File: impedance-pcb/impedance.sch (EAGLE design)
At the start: 26 parts, among them U3 ADG704BRMZ, U4 ADG787BRMZ, U5 RED

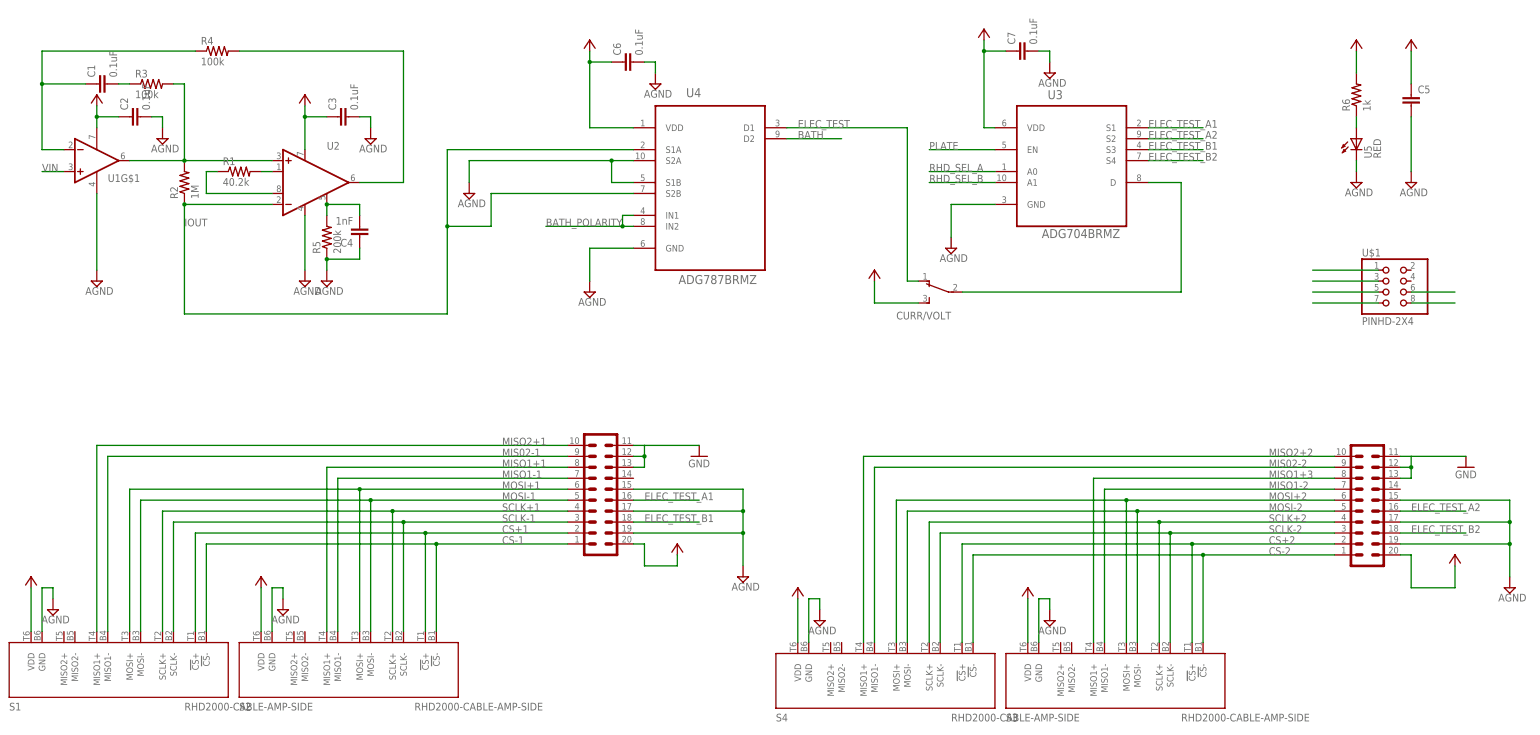
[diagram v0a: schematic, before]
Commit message: Created plating/impedance testing circuit. Need to get parts to prototype it.
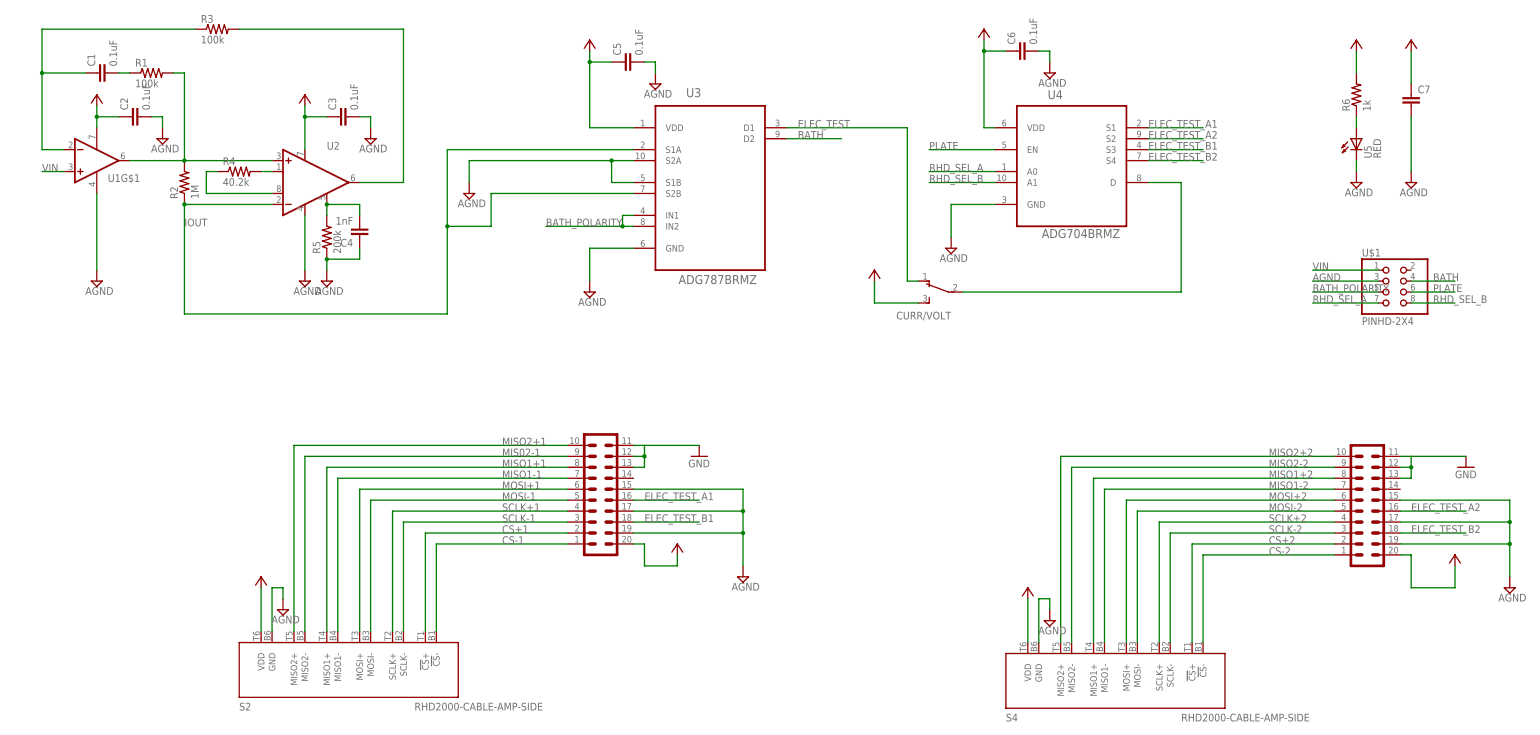
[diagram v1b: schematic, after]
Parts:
- removed S1, S3: RHD2000-CABLE-AMP-SIDE, RHD2000:RHD2000-CABLE-AMP-SIDE
- C5: value (none) -> 0.1uF; device impedance:C_1206 -> impedance:C_0805
- C7: value 0.1uF -> (none); device impedance:C_0805 -> impedance:C_1206
- R1: value 40.2k -> 100k
- R4: value 100k -> 40.2k
- U3: value ADG704BRMZ -> ADG787BRMZ; device impedance:ADG704BRMZ -> impedance:ADG787BRMZ
- U4: value ADG787BRMZ -> ADG704BRMZ; device impedance:ADG787BRMZ -> impedance:ADG704BRMZ
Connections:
- removed net MIS02-2: HS2.9, S4.MISO1-
- removed net MISO1+3: HS2.8, S3.MISO1+
- new net MISO1+2: HS2.8, S4.MISO1+
- new net MISO2-2: HS2.9, S4.MISO2-
- net +3.3V: now also C7.1, S4.VDD; no longer C5.1, S3.VDD
- net +3.3V1: now also C5.1, U3.VDD; no longer C6.1, U4.VDD
- net +3.3V2: now also C6.1, U4.VDD; no longer C7.1, U3.VDD
- net AGND: now also S4.GND, U3.S1B, U3.S2A; no longer S3.GND, U4.S1B, U4.S2A
- net BATH: now also U$1.4, U3.D2; no longer U4.D2
- net BATH_POLARITY: now also U3.IN1, U3.IN2; no longer U4.IN1, U4.IN2
- net CS+1: no longer S1.!CS!+
- net CS+2: no longer S3.!CS!+
- net CS-1: no longer S1.!CS!-
- net CS-2: no longer S3.!CS!-
- net ELEC_TEST: now also U3.D1; no longer U4.D1
- net ELEC_TEST_A1: now also U4.S1; no longer U3.S1
- net ELEC_TEST_A2: now also U4.S2; no longer U3.S2
- net ELEC_TEST_B1: now also U4.S3; no longer U3.S3
- net ELEC_TEST_B2: now also U4.S4; no longer U3.S4
- net IOUT: now also U3.S1A, U3.S2B; no longer U4.S1A, U4.S2B
- net MIS02-1: now also S2.MISO2-; no longer S1.MISO1-
- net MISO1-2: now also S4.MISO1-; no longer S3.MISO1-
- net MISO2+1: now also S2.MISO2+; no longer S1.MISO1+
- net MISO2+2: now also S4.MISO2+; no longer S4.MISO1+
- net MOSI+1: no longer S1.MOSI+
- net MOSI+2: no longer S3.MOSI+
- net MOSI-1: no longer S1.MOSI-
- net MOSI-2: no longer S3.MOSI-
- net N$1: now also R1.2; no longer R3.2
- net N$2: now also R4.2; no longer R1.2
- net N$3: now also R4.1; no longer R1.1
- net N$4: now also R1.1; no longer R3.1
- net N$5: now also R3.1; no longer R4.1
- net N$6: now also R3.2; no longer R4.2
- net N$8: now also U4.D; no longer U3.D
- net PLATE: now also U4.EN; no longer U3.EN
- net RHD_SEL_A: now also U4.A0; no longer U3.A0
- net RHD_SEL_B: now also U4.A1; no longer U3.A1
- net SCLK+1: no longer S1.SCLK+
- net SCLK+2: no longer S3.SCLK+
- net SCLK-1: no longer S1.SCLK-
- net SCLK-2: no longer S3.SCLK-
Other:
- moved on the sheet: C1, C5, C6, C7, R1, R3, R4, S4, U3, U4

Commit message: Updated the impedance test interface schematic based on testing.
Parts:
- removed R2: 1M, impedance:R_0805
- removed U$1: PINHD-2X4, impedance:PINHD-2X4
- added I/0: SCREW10_0.1-THRU, impedance:SCREW10_0.1-THRU
- added R10: 3.3k, impedance:R_0805
- added R7: 3.3M, impedance:R_0805
- added R8: 330k, impedance:R_0805
- added R9: 33k, impedance:R_0805
- added S1: RSER, impedance:SP4T_C-K-R-SERIES
- added U$2: DUAL-POST_BANANA, impedance:DUAL-POST_BANANA
- C1: value 0.1uF -> 10nF
- C7: value (none) -> 10uF
- U1: value (none) -> OPA333
- U2: value (none) -> INA326
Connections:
- removed net +3.3V1: C5.1, U3.VDD
- removed net +3.3V2: C6.1, U4.VDD
- removed net N$8: CURR/VOLT.2, U4.D
- new net N$10: CURR/VOLT.1, R10.1, R7.1, R8.1, R9.1, U2.-IN
- new net N$11: R10.2, S1.4
- new net N$12: R9.2, S1.3
- new net N$13: R8.2, S1.2
- new net N$14: R7.2, S1.1
- new net N$15: U$2.2, U3.D2
- net +3.3V: now also C5.1, C6.1, I/0.2, U3.VDD, U4.VDD; no longer CURR/VOLT.3
- net AGND: now also I/0.10, I/0.3, I/0.9; no longer U$1.3
- net BATH: now also I/0.4, U$2.1; no longer U$1.4, U3.D2
- net BATH_POLARITY: now also I/0.5; no longer U$1.5
- net ELEC_TEST: now also U4.D; no longer CURR/VOLT.1
- net IOUT: now also CURR/VOLT.2; no longer R2.1, U2.-IN
- net N$1: now also S1.COM; no longer R2.2
- net PLATE: now also I/0.6; no longer U$1.6
- net RHD_SEL_A: now also I/0.7; no longer U$1.7
- net RHD_SEL_B: now also I/0.8; no longer U$1.8
- net VIN: now also CURR/VOLT.3, I/0.1; no longer U$1.1
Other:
- note added: "0-0.1uA"
- note added: "0-100uA"
- note added: "0-10uA"
- note added: "0-1uA"
- note added: "0-3.3V"
- note added: "10X"
- note added: "Current range select"
- note added: "Current- or voltage-controlled plating"
- note added: "Impedance Measurement and Electrode Plating Interface for RHD2000 Chips"
- note added: "Meter posts (short if not in use)"
- note added: "Plating polarity selection"
- note added: "Precision voltage-controlled current source"
- note added: "RHD Chip Selection"
- moved on the sheet: C1, C2, C3, C4, C5, C6, C7, CURR/VOLT, R1, R3, R4, R5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

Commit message: Minor.
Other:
- note added: "RHD chip selection"
- note removed: "RHD Chip Selection"
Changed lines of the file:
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@@
 <setting verticaltext="up"/>
 </settings>
-<grid distance="0.1" unitdist="inch" unit="inch" style="lines" multiple="1" display="yes" altdistance="0.01" altunitdist="inch" altunit="inch"/>
+<grid distance="0.1" unitdist="inch" unit="inch" style="lines" multiple="1" display="no" altdistance="0.01" altunitdist="inch" altunit="inch"/>
 <layers>
 <layer number="1" name="Top" color="4" fill="1" visible="no" active="no"/>
@@
 Plating Interface for RHD2000 Chips</text>
 <text x="121.92" y="7.62" size="1.778" layer="97">Plating polarity selection</text>
-<text x="210.82" y="17.78" size="1.778" layer="97">RHD Chip Selection</text>
+<text x="210.82" y="17.78" size="1.778" layer="97">RHD chip selection</text>
 <wire x1="-73.66" y1="104.14" x2="-73.66" y2="66.04" width="0.1524" layer="97" style="shortdash"/>
 <wire x1="-73.66" y1="66.04" x2="-66.04" y2="66.04" width="0.1524" layer="97" style="shortdash"/>
